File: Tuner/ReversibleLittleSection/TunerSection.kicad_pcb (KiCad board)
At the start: 2 copper layers, 100 x 100 mm, 118 parts, among them J1 Conn_01x03, J10 Conn_01x02, J11 Conn_02x05_Odd_Even, J12 Conn_01x01, J13 Conn_01x01, J14 Conn_01x01, J15 Conn_01x01, J16 Conn_01x01, J17 Conn_01x01, J18 Conn_01x01, J19 Conn_01x01, J2 Conn_01x03, J20 Conn_01x01, J21 Conn_01x01, J22 Conn_01x01, J3 Conn_01x03, J4 Conn_01x03, J5 Conn_01x03, J6 Conn_01x03, J7 Conn_01x03, J8 Conn_01x02, J9 Conn_01x02, P10 Conn_01x01, P11 Conn_01x01, P12 Conn_01x01, P2 Conn_01x01, P3 Conn_01x01, P4 Conn_01x01, P5 Conn_01x01, P6 Conn_01x01, P7 Conn_01x01, P8 Conn_01x01, P9 Conn_01x01, U1 MCP23008, U2 ULN2803A

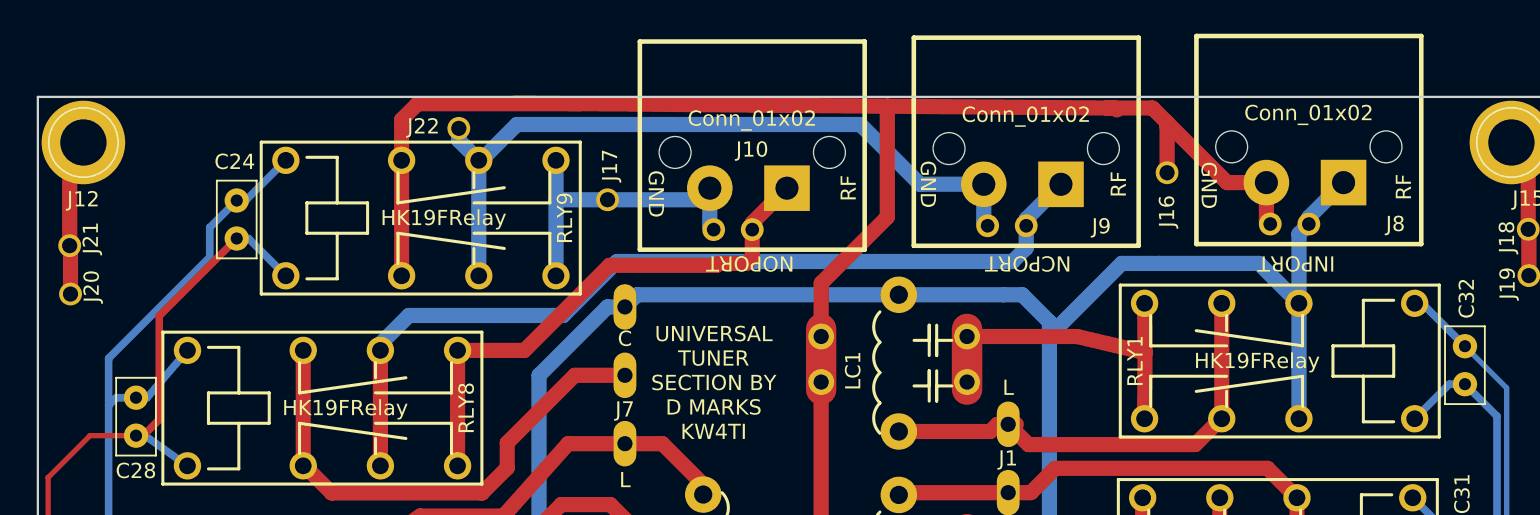
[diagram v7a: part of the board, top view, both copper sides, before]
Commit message: Added nonswitched output to ReversibleSections
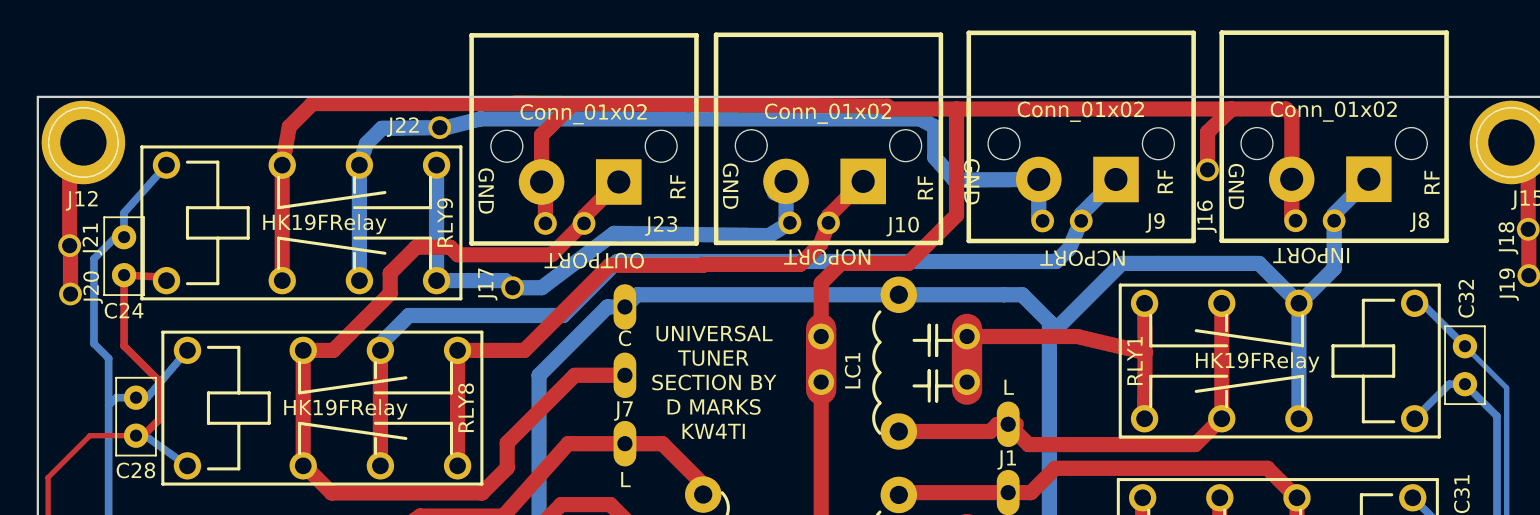
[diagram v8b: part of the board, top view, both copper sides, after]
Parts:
- added J23: Conn_01x02, tuner:bnc_90_1-1337543-0_pad_combo, F.Cu at (86.0, 45.9)
- moved J17 8.52 mm to (82.5, 62.6)
- moved RLY9 7.87 mm to (60.8, 58.3)
- moved C24 7.80 mm to (55.7, 59.2)
- moved J10 5.04 mm to (102.0, 45.9)
- moved J9 3.63 mm to (118.7, 45.8)
- moved J16 2.67 mm to (128.3, 54.8)
- moved J8 1.68 mm to (135.3, 45.8)
- moved J22 1.25 mm to (77.7, 52.0)
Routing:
- net Net-(J23-Pad1): track 33.7 -> 60.5 mm
- net RFGND: track 161.7 -> 186.7 mm
- net Net-(J10-Pad2): track 20.9 -> 36.4 mm
- net Net-(J22-Pad1): track 48.9 -> 59.5 mm
- net RLY8: track 180.3 -> 175.3 mm
- net Net-(J10-Pad1): track 35.0 -> 39.6 mm
- net Net-(J9-Pad1): track 58.4 -> 61.8 mm
- net RLYPWR: track 353.9 -> 351.0 mm
- net RFPORT1: track 169.0 -> 169.9 mm
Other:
- board text added: "OUTPORT"
